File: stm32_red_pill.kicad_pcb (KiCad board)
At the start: 2 copper layers, 59 x 31 mm, 29 parts, among them J1 USB_B_Micro, J2 Conn_01x18, J3 Conn_01x18, SW1 SW_SPDT, U1 STM32F103C8T6, U2 AMS1117-3.3, Y1 16MHZ

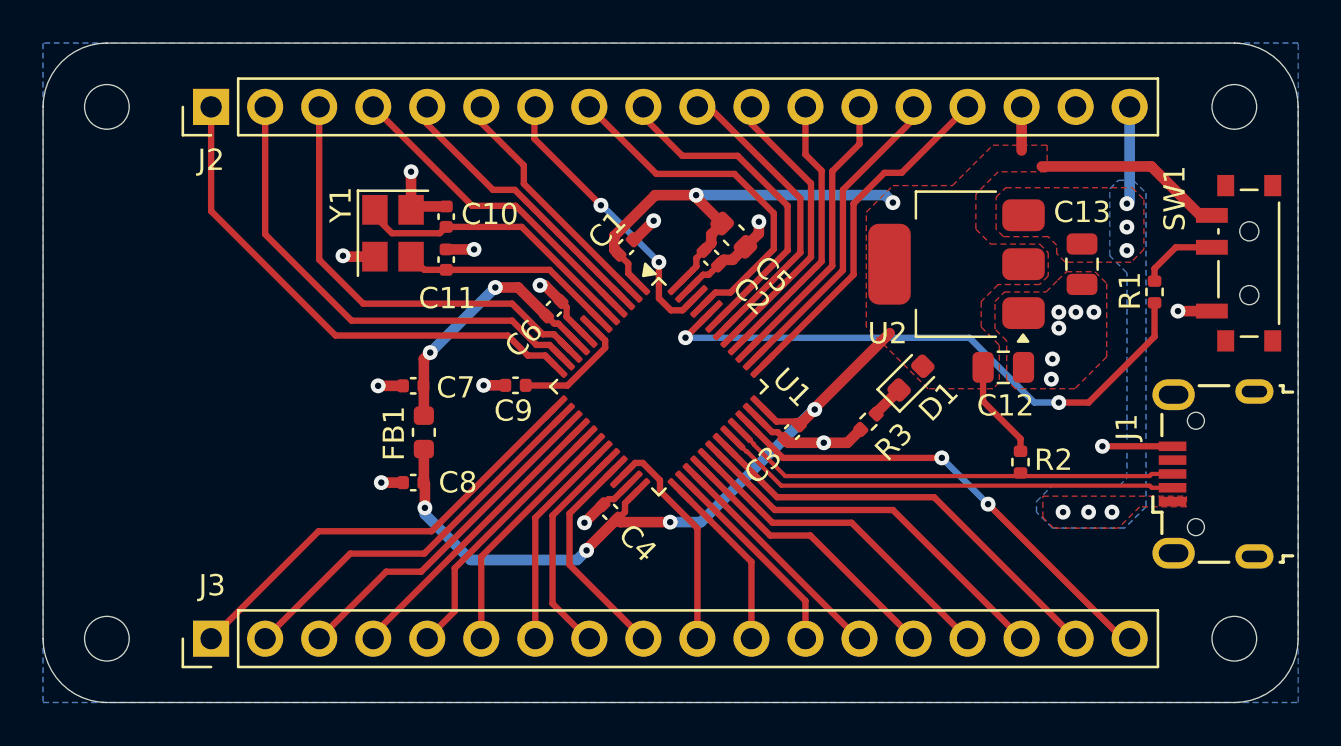
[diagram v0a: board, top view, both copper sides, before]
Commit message: update transformer
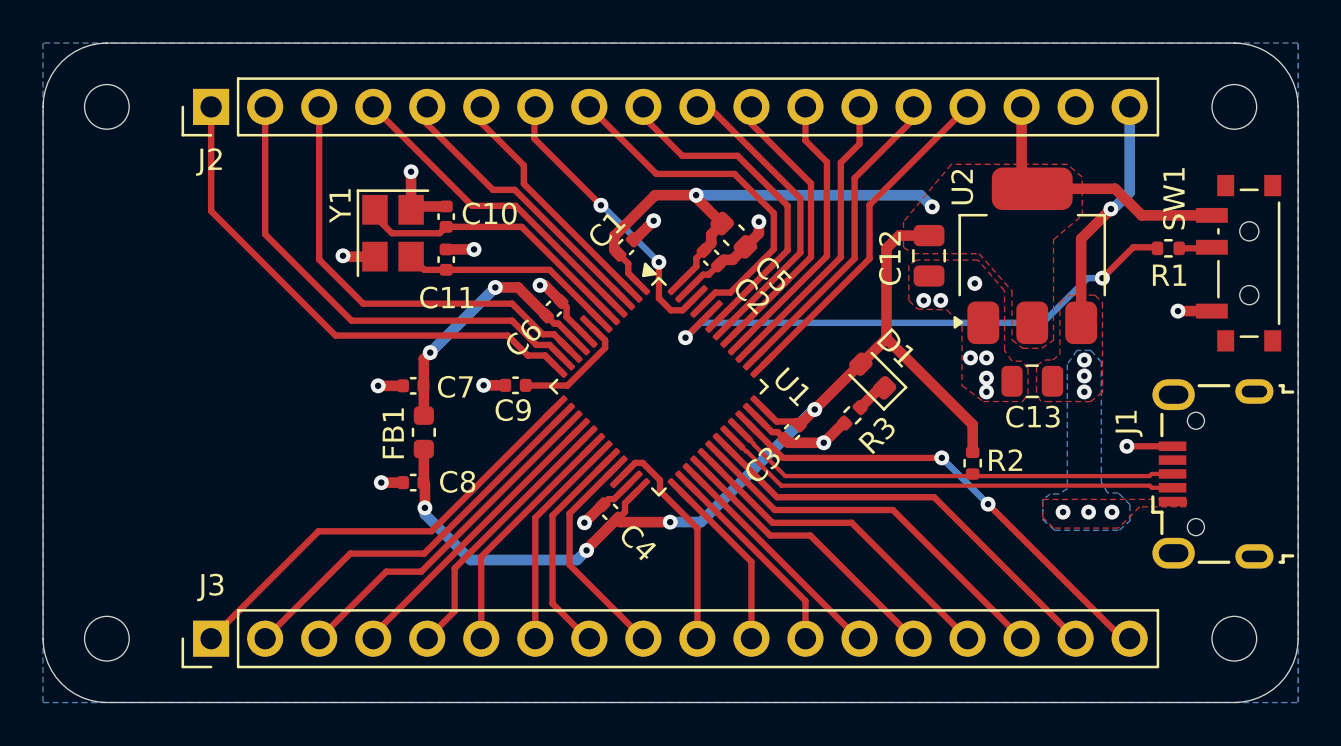
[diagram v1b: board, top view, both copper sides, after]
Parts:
- moved C12 6.30 mm to (121.7, 96.0), turned to -90 degrees
- moved C13 5.98 mm to (126.5, 101.9), turned to 180 degrees
- moved U2 3.58 mm to (126.5, 96.0), turned to 90 degrees
- moved R2 2.25 mm to (123.7, 105.8)
- moved R1 2.15 mm to (132.9, 95.7), turned to 180 degrees
- moved D1 1.80 mm to (119.0, 101.7), turned to 135 degrees
- moved R3 0.81 mm to (118.0, 103.5)
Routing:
- net +3.3V: track 74.4 -> 85.7 mm
- net VBUS: track 4.60 -> 11.2 mm, vias 6 -> 7
- net /BOOT0: track 27.8 -> 25.6 mm
- net /SW_BOOT0: track 3.70 -> 1.56 mm
- net GND: track 32.8 -> 30.9 mm, vias 19 -> 20
